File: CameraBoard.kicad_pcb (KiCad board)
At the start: 2 copper layers, 65 x 35 mm, 7 parts, among them J1 CAMERA, J2 MOTION, J3 CAMERA+MOTION

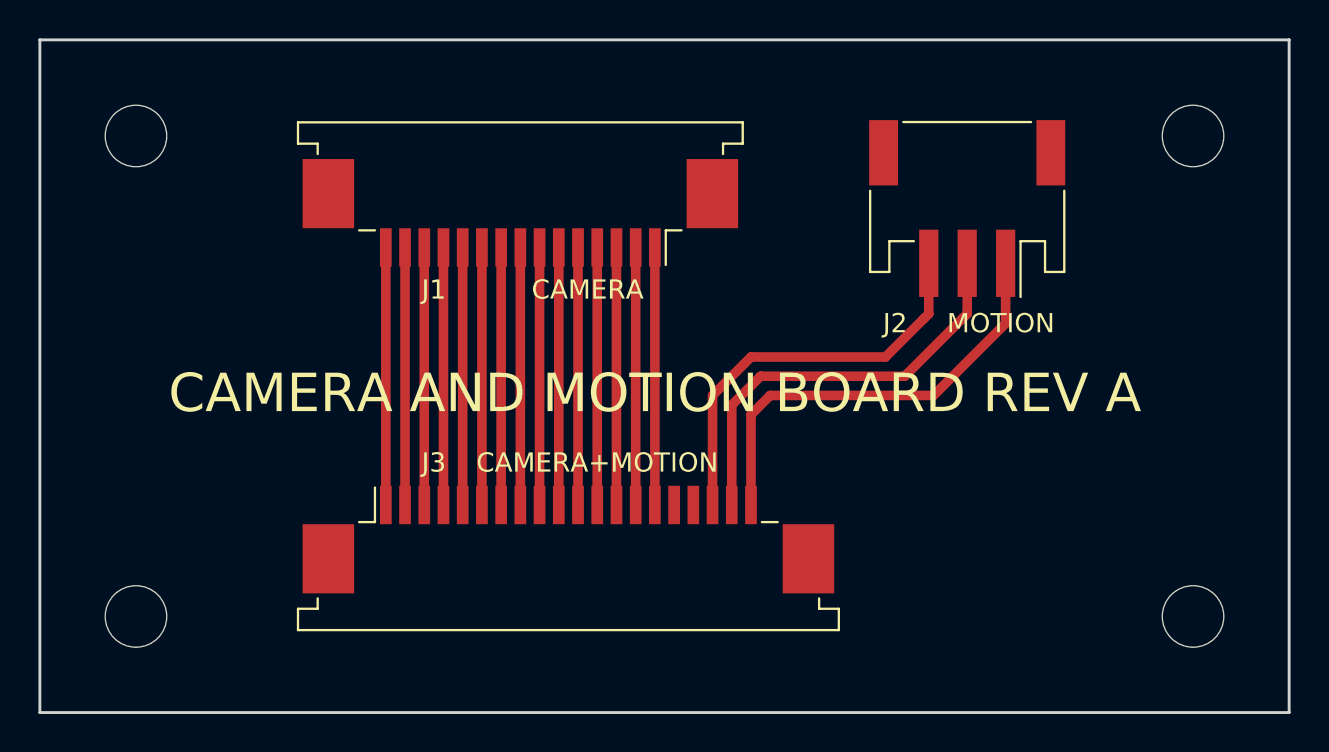
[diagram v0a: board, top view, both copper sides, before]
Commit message: PCB smaller Rev A
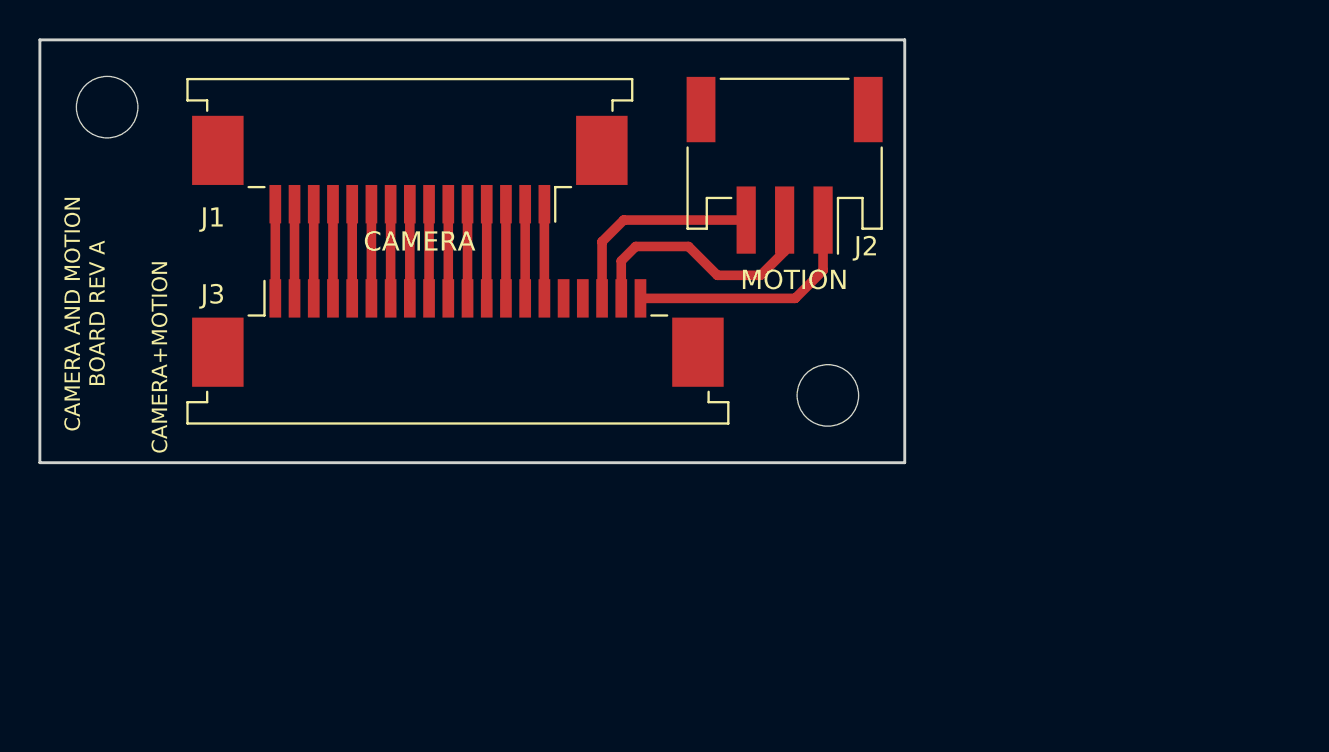
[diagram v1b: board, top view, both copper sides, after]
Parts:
- removed the REF** at (105.0, 130.0)
- removed the REF** at (160.0, 105.0)
- moved REF** 22.2 mm to (141.0, 118.5)
- moved J3 12.2 mm to (121.8, 115.2)
- moved J2 9.76 mm to (138.8, 106.5)
- moved J1 6.17 mm to (119.2, 106.8)
- moved REF** 2.12 mm to (103.5, 103.5)
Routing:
- net Net-(J2-Pad3): track 21.3 -> 10.9 mm
- net Net-(J2-Pad1): track 23.0 -> 12.7 mm
- net Net-(J2-Pad2): track 22.0 -> 13.5 mm
- net Net-(J1-Pad9): track 13.4 -> 4.90 mm
- net Net-(J1-Pad8): track 13.4 -> 4.90 mm
- net Net-(J1-Pad7): track 13.4 -> 4.90 mm
- net Net-(J1-Pad6): track 13.4 -> 4.90 mm
- net Net-(J1-Pad5): track 13.4 -> 4.90 mm
- net Net-(J1-Pad4): track 13.4 -> 4.90 mm
- net Net-(J1-Pad3): track 13.4 -> 4.90 mm
- net Net-(J1-Pad2): track 13.4 -> 4.90 mm
- net Net-(J1-Pad15): track 13.4 -> 4.90 mm
- net Net-(J1-Pad14): track 13.4 -> 4.90 mm
- net Net-(J1-Pad13): track 13.4 -> 4.90 mm
- net Net-(J1-Pad12): track 13.4 -> 4.90 mm
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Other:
- board size 65 x 35 mm -> 45 x 22 mm
